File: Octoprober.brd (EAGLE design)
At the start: 130.8 x 91.7 mm, 143 parts, among them J1 10118193-0001LF, J2 26-60-4020, SW1 101-0134-EV, SW2 EVQ-Q2203W, SW3 EVQ-Q2203W, SW4 EVQ-Q2203W, SW5 EVQ-Q2203W, U1 P8X32A-M44, U10 MAX31855KASA+, U11 MAX31855KASA+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

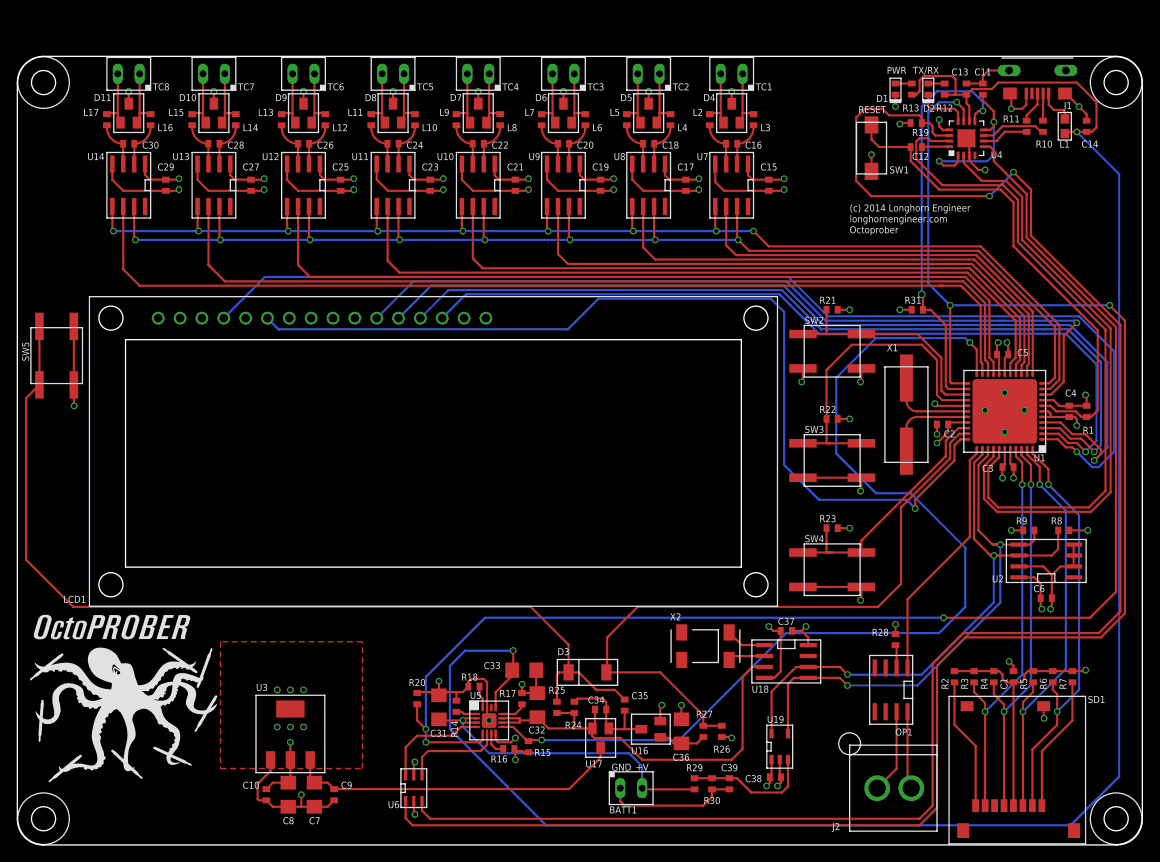
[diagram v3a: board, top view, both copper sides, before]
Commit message: Added cap to FT230X RST line.
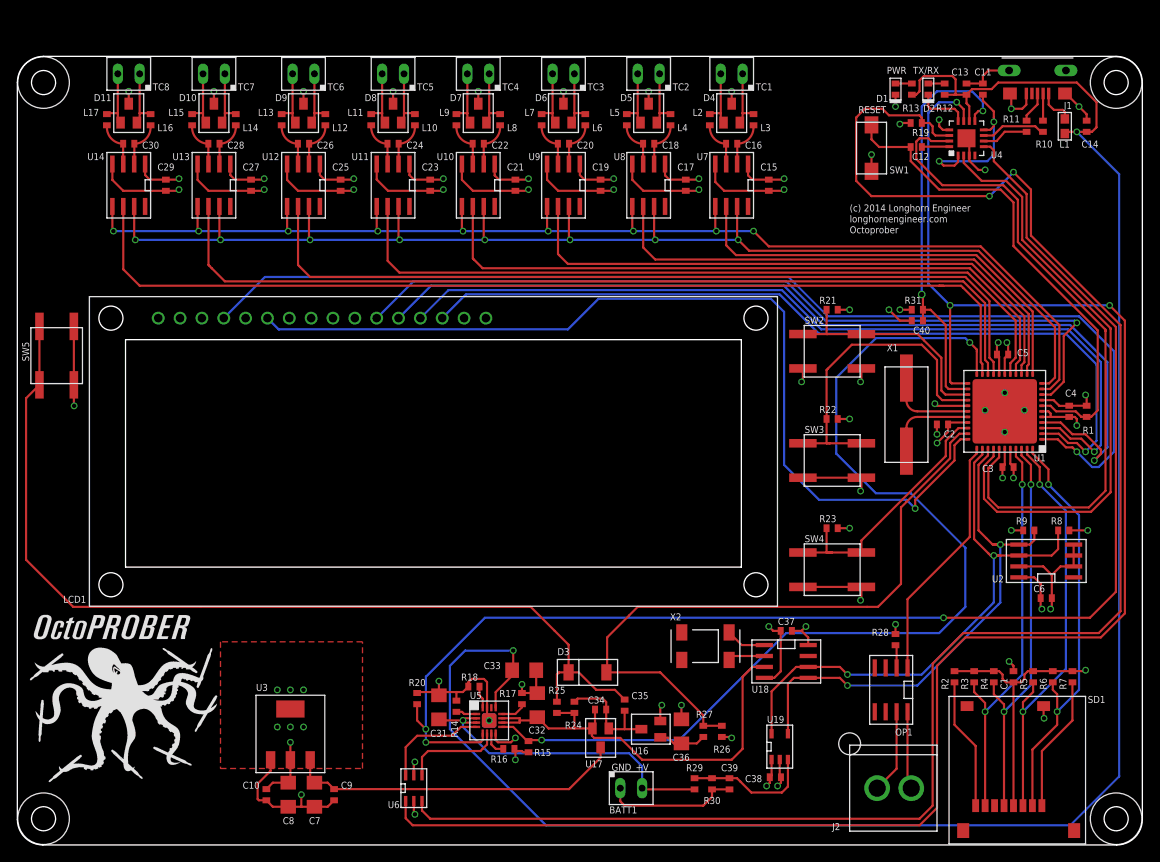
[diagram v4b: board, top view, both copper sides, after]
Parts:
- added C40: 0.1uF, PP_Passives:0402
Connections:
- net FT230_RST: now also C40.1
- net GND: now also C40.2
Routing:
- net GND: track 389.2 -> 392.6 mm, vias 49 -> 50
- net FT230_RST: track 48.1 -> 49.4 mm
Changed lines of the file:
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@@
 </element>
 <element name="R31" library="PP_Passives" package="0402" value="10K" x="104.648" y="62.23"/>
+<element name="C40" library="PP_Passives" package="0402" value="0.1uF" x="104.648" y="60.96" rot="R180"/>
 </elements>
 <signals>
@@
 <contactref element="LCD1" pad="1"/>
 <wire x1="29.45" y1="9.906" x2="29.45" y2="8.622" width="0.254" layer="1"/>
-<wire x1="29.45" y1="8.622" x2="28.194" y2="7.366" width="0.254" layer="1"/>
-<wire x1="28.194" y1="7.366" x2="27.94" y2="7.112" width="0.254" layer="1"/>
+<wire x1="29.45" y1="8.622" x2="27.94" y2="7.112" width="0.254" layer="1"/>
 <wire x1="27.94" y1="7.112" x2="27.94" y2="5.334" width="0.254" layer="1"/>
 <wire x1="27.94" y1="5.334" x2="28.082" y2="5.192" width="0.254" layer="1"/>
 <wire x1="28.082" y1="5.192" x2="28.956" y2="5.192" width="0.254" layer="1"/>
+<contactref element="C40" pad="2"/>
+<wire x1="103.998" y1="60.96" x2="102.616" y2="60.96" width="0.254" layer="1"/>
+<wire x1="102.616" y1="60.96" x2="101.346" y2="62.23" width="0.254" layer="1"/>
+<via x="101.346" y="62.23" extent="1-16" drill="0.5"/>
+<wire x1="101.346" y1="62.23" x2="101.346" y2="62.484" width="0.254" layer="2"/>
 </signal>
 <signal name="RES">
@@
 <wire x1="110.508" y1="53.019" x2="108.271" y2="53.019" width="0.254" layer="1"/>
 <wire x1="108.271" y1="53.019" x2="107.95" y2="53.34" width="0.254" layer="1"/>
-<wire x1="107.95" y1="53.34" x2="107.95" y2="58.928" width="0.254" layer="1"/>
+<wire x1="107.95" y1="53.34" x2="107.95" y2="60.452" width="0.254" layer="1"/>
 <contactref element="U4" pad="9"/>
 <contactref element="R31" pad="2"/>
-<wire x1="107.95" y1="58.928" x2="107.95" y2="60.452" width="0.254" layer="1"/>
 <wire x1="107.95" y1="60.452" x2="106.172" y2="62.23" width="0.254" layer="1"/>
 <wire x1="106.172" y1="62.23" x2="105.298" y2="62.23" width="0.254" layer="1"/>
@@
 <via x="112.268" y="85.344" extent="1-16" drill="0.5"/>
 <wire x1="112.268" y1="85.344" x2="111.76" y2="85.344" width="0.254" layer="1"/>
-<wire x1="111.76" y1="85.344" x2="111.506" y2="85.09" width="0.254" layer="1"/>
-<wire x1="111.506" y1="85.09" x2="111.338" y2="84.922" width="0.254" layer="1"/>
+<wire x1="111.76" y1="85.344" x2="111.338" y2="84.922" width="0.254" layer="1"/>
 <wire x1="111.338" y1="84.922" x2="111.338" y2="84.169" width="0.254" layer="1"/>
+<contactref element="C40" pad="1"/>
+<wire x1="105.298" y1="60.96" x2="105.298" y2="62.23" width="0.254" layer="1"/>
 </signal>
 <signal name="S_P_G">

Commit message: Fixed screw terminal footprints.
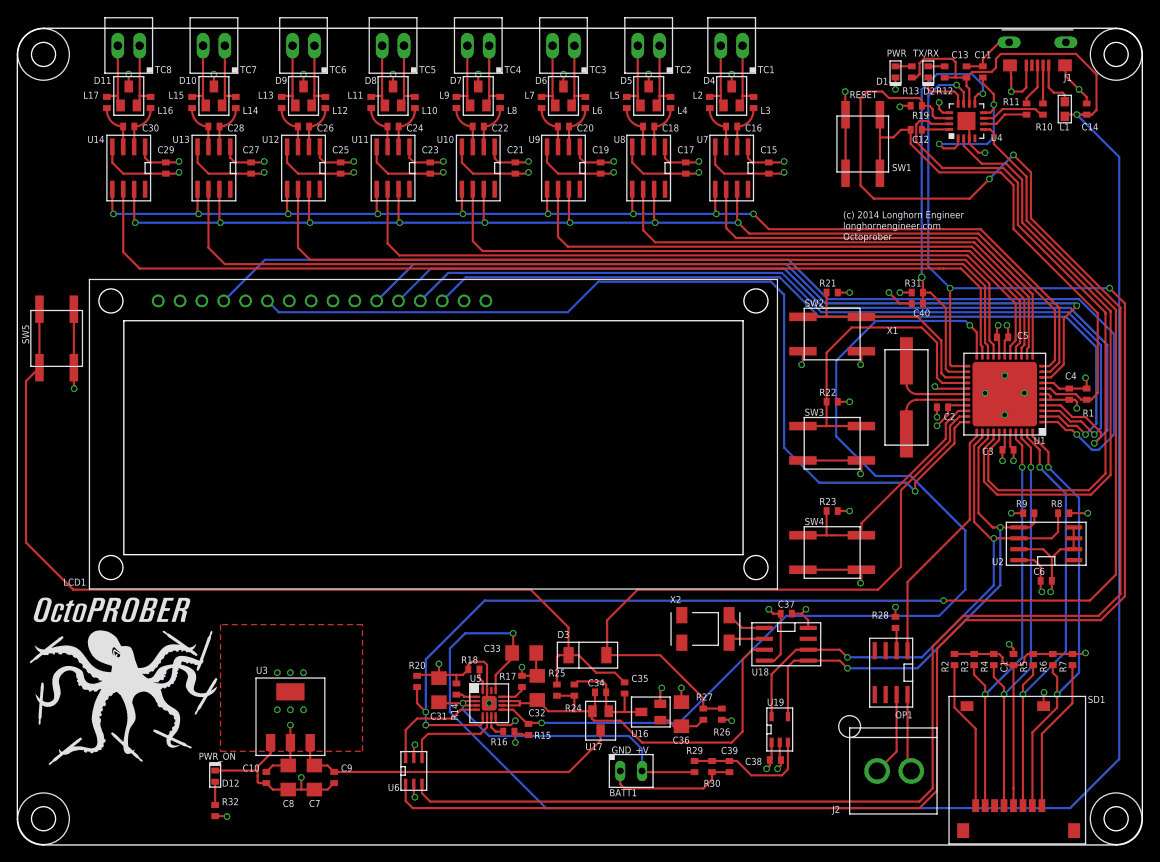
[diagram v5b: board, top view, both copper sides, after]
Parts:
- added D12: 598-8070-107F, PP_LED:LED_0402
- added R32: 330, PP_Passives:0402
- SW1: value 101-0134-EV -> EVQ-Q2203W; device PP_Electromechanical:101-0134-EV -> PP_Electromechanical:EVQ-Q2203W
- TC1, TC2, TC3, TC4, TC5, TC6, TC7, TC8: device PP_Connectors:HEADER_01X02_PTH -> PP_Connectors:HEADER_01X02_PTH_SCREWTERM
- moved J1 3.27 mm to (118.6, 93.2)
- moved TC1 3.27 mm to (84.3, 92.9)
- moved TC2 3.27 mm to (74.7, 92.9)
- moved TC3 3.27 mm to (64.8, 92.9)
- moved TC4 3.27 mm to (54.9, 92.9)
- moved TC5 3.27 mm to (45.0, 92.9)
- moved TC6 3.27 mm to (34.5, 92.9)
- moved TC7 3.27 mm to (24.1, 92.9)
- moved TC8 3.27 mm to (14.2, 92.9)
- moved U$3 3.27 mm to (3.05, 91.9)
- moved U$4 3.27 mm to (127.8, 91.9)
- moved LCD1 2.00 mm to (8.38, 65.8)
- moved R21 2.00 mm to (94.7, 64.2)
- moved R31 2.00 mm to (104.6, 64.2)
- moved C34 2.00 mm to (67.8, 17.7)
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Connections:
- new net N$22: D12.ANODE, R32.2
- net 3.3V: now also R32.1
- net GND: now also D12.CATHODE, SW1.2
- net RES: now also SW1.3, SW1.4; no longer SW1.2
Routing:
- net GND: track 392.6 -> 410.5 mm
- net RES: track 57.8 -> 61.9 mm
- net 3.3V: track 257.1 -> 261.0 mm, vias 34 -> 35
- net N$22: track 0.00 -> 2.70 mm
- net !PWREN: track 199.5 -> 202.0 mm
- net USB_V1: track 225.3 -> 227.7 mm
- net SD_SCLK: track 47.2 -> 49.2 mm
- net SD_DO: track 47.6 -> 49.6 mm
- net SD_DI: track 49.4 -> 51.4 mm
- net IRQ: track 15.4 -> 17.4 mm
- net SD_RW: track 15.8 -> 17.8 mm
- net SD_CS: track 49.6 -> 51.6 mm
- net N$2: track 7.12 -> 8.39 mm
- net D-: track 3.17 -> 4.44 mm
- net N$9: track 7.37 -> 8.64 mm
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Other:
- board size 130.8 x 91.7 mm -> 130.8 x 95 mm
- board text added: "PWR_ON"

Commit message: LCD Screen is Serial now.
Wrote spin code for Serial interface.
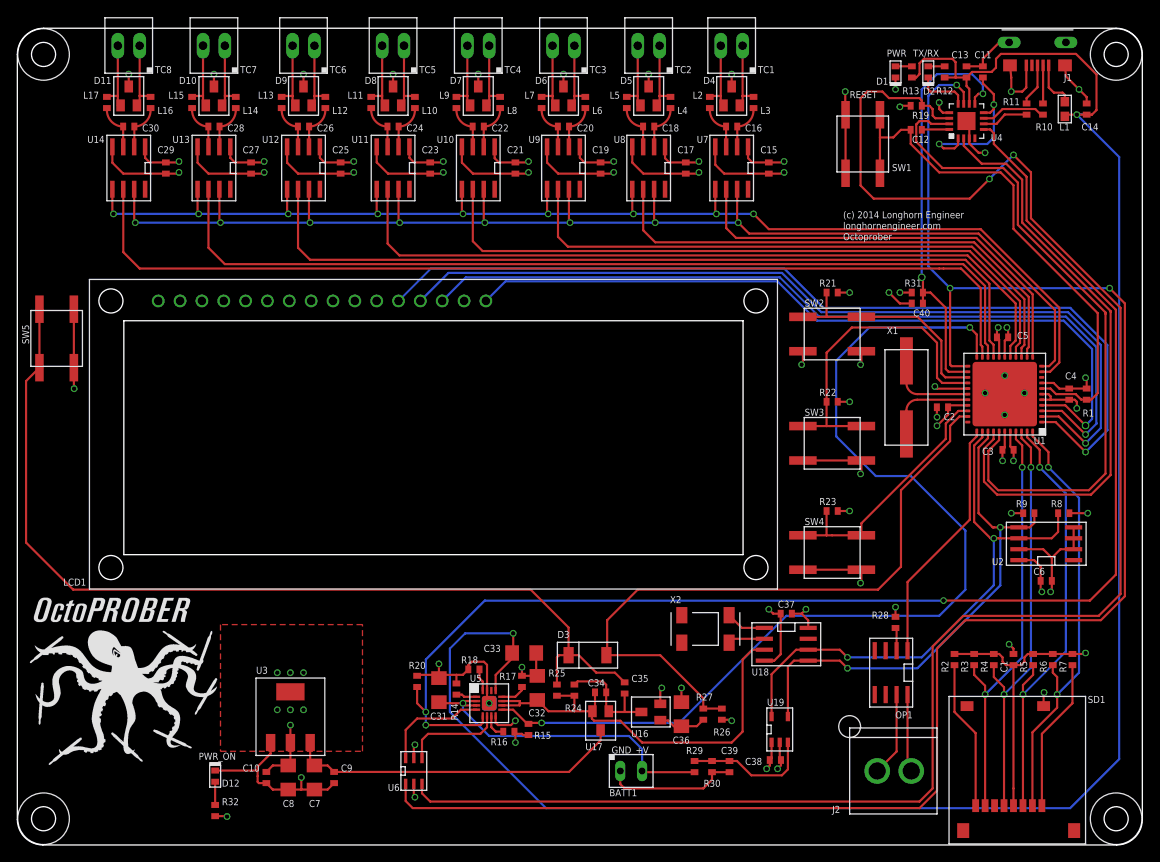
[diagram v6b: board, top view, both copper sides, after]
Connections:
- removed net BK_GND: LCD1.16
- removed net CONTRAST: LCD1.3
- removed net LCD_D4: LCD1.11, U1.9
- removed net LCD_D5: LCD1.12, U1.4
- removed net LCD_D6: LCD1.13, U1.3
- removed net LCD_D7: LCD1.14, U1.2
- removed net LCD_E: LCD1.6, U1.33
- removed net LCD_RS: LCD1.4, U1.1
- new net LCD_CS: LCD1.16, U1.4
- new net LCD_SCL: LCD1.12, U1.1
- new net LCD_SDI: LCD1.14, U1.3
- new net LCD_SDO: LCD1.13, U1.2
- new net P26: U1.33
- new net P8: U1.9
- net 3.3V: no longer LCD1.15
- net GND: no longer LCD1.5
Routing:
- net LCD_RS: track 131.2 -> 0.00 mm, vias 1 -> 0
- net LCD_D5: track 109.5 -> 0.00 mm, vias 1 -> 0
- net LCD_E: track 108.9 -> 0.00 mm, vias 1 -> 0
- net LCD_SCL: track 0.00 -> 107.7 mm, vias 0 -> 1
- net LCD_SDO: track 0.00 -> 102.5 mm, vias 0 -> 1
- net LCD_D6: track 101.9 -> 0.00 mm, vias 1 -> 0
- net LCD_SDI: track 0.00 -> 97.5 mm, vias 0 -> 1
- net LCD_D7: track 97.2 -> 0.00 mm, vias 1 -> 0
- net LCD_D4: track 95.8 -> 0.00 mm, vias 1 -> 0
- net LCD_CS: track 0.00 -> 90.0 mm, vias 0 -> 1
- net CHARGING: track 117.9 -> 117.2 mm

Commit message: Added code for Reset function.
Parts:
- added R33: 10K, PP_Passives:0402
- moved SW1 1.02 mm to (98.3, 80.5)
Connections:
- removed net P8: U1.9
- new net USB_RST: C12.2, R33.2, SW1.1, SW1.2, U1.9
- net 3.3V: now also R33.1
- net GND: no longer SW1.1, SW1.2
- net RES: no longer C12.2
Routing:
- net USB_RST: track 0.00 -> 63.9 mm
- net GND: track 410.2 -> 400.2 mm, vias 50 -> 49
- net !PWREN: track 202.0 -> 196.2 mm
- net 3.3V: track 261.0 -> 263.4 mm, vias 35 -> 36
- net RES: track 61.9 -> 59.9 mm
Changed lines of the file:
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@@
 <element name="R31" library="PP_Passives" package="0402" value="10K" x="104.648" y="64.23"/>
 <element name="C40" library="PP_Passives" package="0402" value="0.1uF" x="104.648" y="62.96" rot="R180"/>
-<element name="SW1" library="PP_Electromechanical" package="EVQ-Q2203W" value="EVQ-Q2203W" x="98.298" y="81.502" smashed="yes" rot="R270">
-<attribute name="NAME" x="101.702" y="78.352" size="0.8128" layer="25" font="vector"/>
+<element name="SW1" library="PP_Electromechanical" package="EVQ-Q2203W" value="EVQ-Q2203W" x="98.298" y="80.486" smashed="yes" rot="R270">
+<attribute name="NAME" x="101.702" y="77.336" size="0.8128" layer="25" font="vector"/>
 </element>
 <element name="D12" library="PP_LED" package="LED_0402" value="598-8070-107F" x="23" y="8" smashed="yes" rot="R270">
@@
 <attribute name="NAME" x="23.785" y="4.6225" size="0.8128" layer="25" font="vector"/>
 </element>
+<element name="R33" library="PP_Passives" package="0402" value="10K" x="123.698" y="60.198" rot="R270"/>
 </elements>
 <signals>
@@
 <via x="101.346" y="64.23" extent="1-16" drill="0.5"/>
 <wire x1="101.346" y1="64.23" x2="101.346" y2="64.484" width="0.254" layer="2"/>
-<contactref element="SW1" pad="2"/>
-<contactref element="SW1" pad="1"/>
-<wire x1="96.298" y1="84.902" x2="96.266" y2="84.902" width="0.254" layer="1"/>
-<wire x1="96.266" y1="84.902" x2="96.266" y2="87.598" width="0.254" layer="1"/>
-<via x="96.266" y="87.598" extent="1-16" drill="0.5"/>
-<wire x1="96.266" y1="87.598" x2="96.266" y2="88.106" width="0.254" layer="2"/>
-<wire x1="96.298" y1="78.102" x2="96.298" y2="84.902" width="0.254" layer="1"/>
 <wire x1="115.318" y1="93.321" x2="114.181" y2="93.321" width="0.254" layer="1"/>
 <wire x1="114.181" y1="93.321" x2="112.268" y2="91.408" width="0.254" layer="1"/>
@@
 <contactref element="U1" pad="7"/>
 <contactref element="R1" pad="1"/>
-<contactref element="C12" pad="2"/>
 <wire x1="119.108" y1="53.069" x2="120.127" y2="53.069" width="0.254" layer="1"/>
 <wire x1="120.127" y1="53.069" x2="120.777" y2="52.419" width="0.254" layer="1"/>
@@
 <wire x1="123.698" y1="51.784" x2="124.318" y2="51.784" width="0.254" layer="1"/>
 <wire x1="124.318" y1="51.784" x2="124.333" y2="51.769" width="0.254" layer="1"/>
-<wire x1="103.871" y1="83.153" x2="103.871" y2="81.517" width="0.254" layer="1"/>
 <wire x1="103.871" y1="81.517" x2="107.188" y2="78.2" width="0.254" layer="1"/>
 <wire x1="107.188" y1="78.2" x2="114.33518125" y2="78.2" width="0.254" layer="1"/>
@@
 <contactref element="SW1" pad="4"/>
 <contactref element="SW1" pad="3"/>
-<wire x1="103.871" y1="83.153" x2="102.743" y2="83.153" width="0.254" layer="1"/>
-<wire x1="102.743" y1="83.153" x2="101.854" y2="82.264" width="0.254" layer="1"/>
-<wire x1="101.854" y1="82.264" x2="100.298" y2="82.264" width="0.254" layer="1"/>
-<wire x1="100.298" y1="82.264" x2="100.298" y2="78.102" width="0.254" layer="1"/>
-<wire x1="100.298" y1="84.902" x2="100.298" y2="82.264" width="0.254" layer="1"/>
+<wire x1="100.298" y1="82.264" x2="100.298" y2="81.534" width="0.254" layer="1"/>
+<wire x1="100.298" y1="81.534" x2="100.298" y2="77.086" width="0.254" layer="1"/>
+<wire x1="100.298" y1="83.886" x2="100.298" y2="82.264" width="0.254" layer="1"/>
+<wire x1="103.871" y1="81.517" x2="103.854" y2="81.534" width="0.254" layer="1"/>
+<wire x1="103.854" y1="81.534" x2="100.298" y2="81.534" width="0.254" layer="1"/>
 </signal>
 <signal name="3.3V">
@@
 <via x="24.384" y="3.302" extent="1-16" drill="0.5"/>
 <wire x1="24.384" y1="3.302" x2="24.892" y2="3.302" width="0.254" layer="15"/>
+<contactref element="R33" pad="1"/>
+<wire x1="123.698" y1="60.848" x2="123.698" y2="62.484" width="0.254" layer="1"/>
+<via x="123.698" y="62.484" extent="1-16" drill="0.5"/>
+<wire x1="123.698" y1="62.484" x2="123.19" y2="62.992" width="0.254" layer="15"/>
 </signal>
 <signal name="SD_RW">
@@
 <wire x1="128.27" y1="29.178" x2="128.27" y2="62.452" width="0.254" layer="1"/>
 <via x="115.824" y="80.232" extent="1-16" drill="0.5"/>
-<wire x1="115.824" y1="80.232" x2="113.03" y2="77.438" width="0.254" layer="16"/>
-<via x="113.03" y="77.438" extent="1-16" drill="0.5"/>
-<wire x1="100.584" y1="87.598" x2="101.346" y2="86.836" width="0.254" layer="1"/>
 <wire x1="101.346" y1="86.836" x2="104.902" y2="86.836" width="0.254" layer="1"/>
 <wire x1="104.902" y1="86.836" x2="105.156" y2="86.582" width="0.254" layer="1"/>
@@
 <wire x1="106.426" y1="23.082" x2="106.426" y2="6.572" width="0.254" layer="1"/>
 <wire x1="106.426" y1="6.572" x2="104.902" y2="5.048" width="0.254" layer="1"/>
-<wire x1="100.584" y1="87.598" x2="98.806" y2="87.598" width="0.254" layer="1"/>
-<wire x1="98.806" y1="87.598" x2="98.044" y2="86.836" width="0.254" layer="1"/>
-<wire x1="98.044" y1="86.836" x2="98.044" y2="76.676" width="0.254" layer="1"/>
-<wire x1="98.044" y1="76.676" x2="99.568" y2="75.152" width="0.254" layer="1"/>
-<wire x1="99.568" y1="75.152" x2="110.744" y2="75.152" width="0.254" layer="1"/>
-<wire x1="110.744" y1="75.152" x2="113.03" y2="77.438" width="0.254" layer="1"/>
+<wire x1="115.824" y1="80.232" x2="114.3" y2="81.756" width="0.254" layer="16"/>
+<wire x1="114.3" y1="81.756" x2="114.3" y2="88.392" width="0.254" layer="16"/>
+<wire x1="114.3" y1="88.392" x2="110.998" y2="91.694" width="0.254" layer="16"/>
+<wire x1="110.998" y1="91.694" x2="101.346" y2="91.694" width="0.254" layer="16"/>
+<wire x1="101.346" y1="91.694" x2="100.33" y2="90.678" width="0.254" layer="16"/>
+<wire x1="100.33" y1="90.678" x2="100.33" y2="90.17" width="0.254" layer="16"/>
+<via x="100.33" y="90.17" extent="1-16" drill="0.5"/>
+<wire x1="100.33" y1="90.17" x2="100.33" y2="87.852" width="0.254" layer="1"/>
+<wire x1="100.33" y1="87.852" x2="101.346" y2="86.836" width="0.254" layer="1"/>
 </signal>
 <signal name="!SLEEP">
@@
 <wire x1="121.855" y1="51.119" x2="119.108" y2="51.119" width="0.254" layer="1"/>
 </signal>
-<signal name="P8">
+<signal name="USB_RST">
+<contactref element="C12" pad="2"/>
+<contactref element="SW1" pad="2"/>
+<contactref element="SW1" pad="1"/>
+<wire x1="96.298" y1="77.086" x2="96.298" y2="83.886" width="0.254" layer="1"/>
+<contactref element="R33" pad="2"/>
+<wire x1="96.298" y1="83.886" x2="96.298" y2="85.884" width="0.254" layer="1"/>
+<wire x1="96.298" y1="85.884" x2="96.774" y2="86.36" width="0.254" layer="1"/>
+<wire x1="96.774" y1="86.36" x2="100.838" y2="86.36" width="0.254" layer="1"/>
+<wire x1="100.838" y1="86.36" x2="101.6" y2="85.598" width="0.254" layer="1"/>
+<wire x1="101.6" y1="85.598" x2="101.6" y2="84.328" width="0.254" layer="1"/>
+<wire x1="101.6" y1="84.328" x2="102.616" y2="83.312" width="0.254" layer="1"/>
+<wire x1="102.616" y1="83.312" x2="102.775" y2="83.153" width="0.254" layer="1"/>
+<wire x1="102.775" y1="83.153" x2="103.871" y2="83.153" width="0.254" layer="1"/>
 <contactref element="U1" pad="9"/>
+<wire x1="119.108" y1="54.369" x2="120.155" y2="54.369" width="0.254" layer="1"/>
+<wire x1="120.155" y1="54.369" x2="122.174" y2="56.388" width="0.254" layer="1"/>
+<wire x1="122.174" y1="56.388" x2="122.174" y2="59.436" width="0.254" layer="1"/>
+<wire x1="122.174" y1="59.436" x2="122.174" y2="63.246" width="0.254" layer="1"/>
+<wire x1="122.174" y1="63.246" x2="111.252" y2="74.168" width="0.254" layer="1"/>
+<wire x1="111.252" y1="74.168" x2="97.028" y2="74.168" width="0.254" layer="1"/>
+<wire x1="97.028" y1="74.168" x2="96.266" y2="74.93" width="0.254" layer="1"/>
+<wire x1="96.266" y1="74.93" x2="96.266" y2="77.054" width="0.254" layer="1"/>
+<wire x1="96.266" y1="77.054" x2="96.298" y2="77.086" width="0.254" layer="1"/>
+<wire x1="123.698" y1="59.548" x2="122.286" y2="59.548" width="0.254" layer="1"/>
+<wire x1="122.286" y1="59.548" x2="122.174" y2="59.436" width="0.254" layer="1"/>
 </signal>
 <signal name="P26">
